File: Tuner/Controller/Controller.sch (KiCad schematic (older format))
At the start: 98 parts, among them J1 Conn_02x05_Odd_Even, J10 Conn_01x05, J11 Conn_Coaxial, J13 Conn_Coaxial, J15 Conn_01x02, J16 Conn_01x08, J18 Conn_01x01, J19 Conn_01x01, J2 Conn_02x05_Odd_Even, J20 Conn_01x01, J21 Conn_01x01, J3 Conn_02x05_Odd_Even, J4 Conn_02x05_Odd_Even, J5 Conn_02x05_Odd_Even, J6 Conn_01x02, J7 Conn_02x05_Odd_Even, J8 Conn_01x06, J9 Conn_Coaxial, Q10 2N7000, Q11 2N7000, Q12 2N7000, Q2 2N3904, Q9 2N7000, U4 LM350_TO220

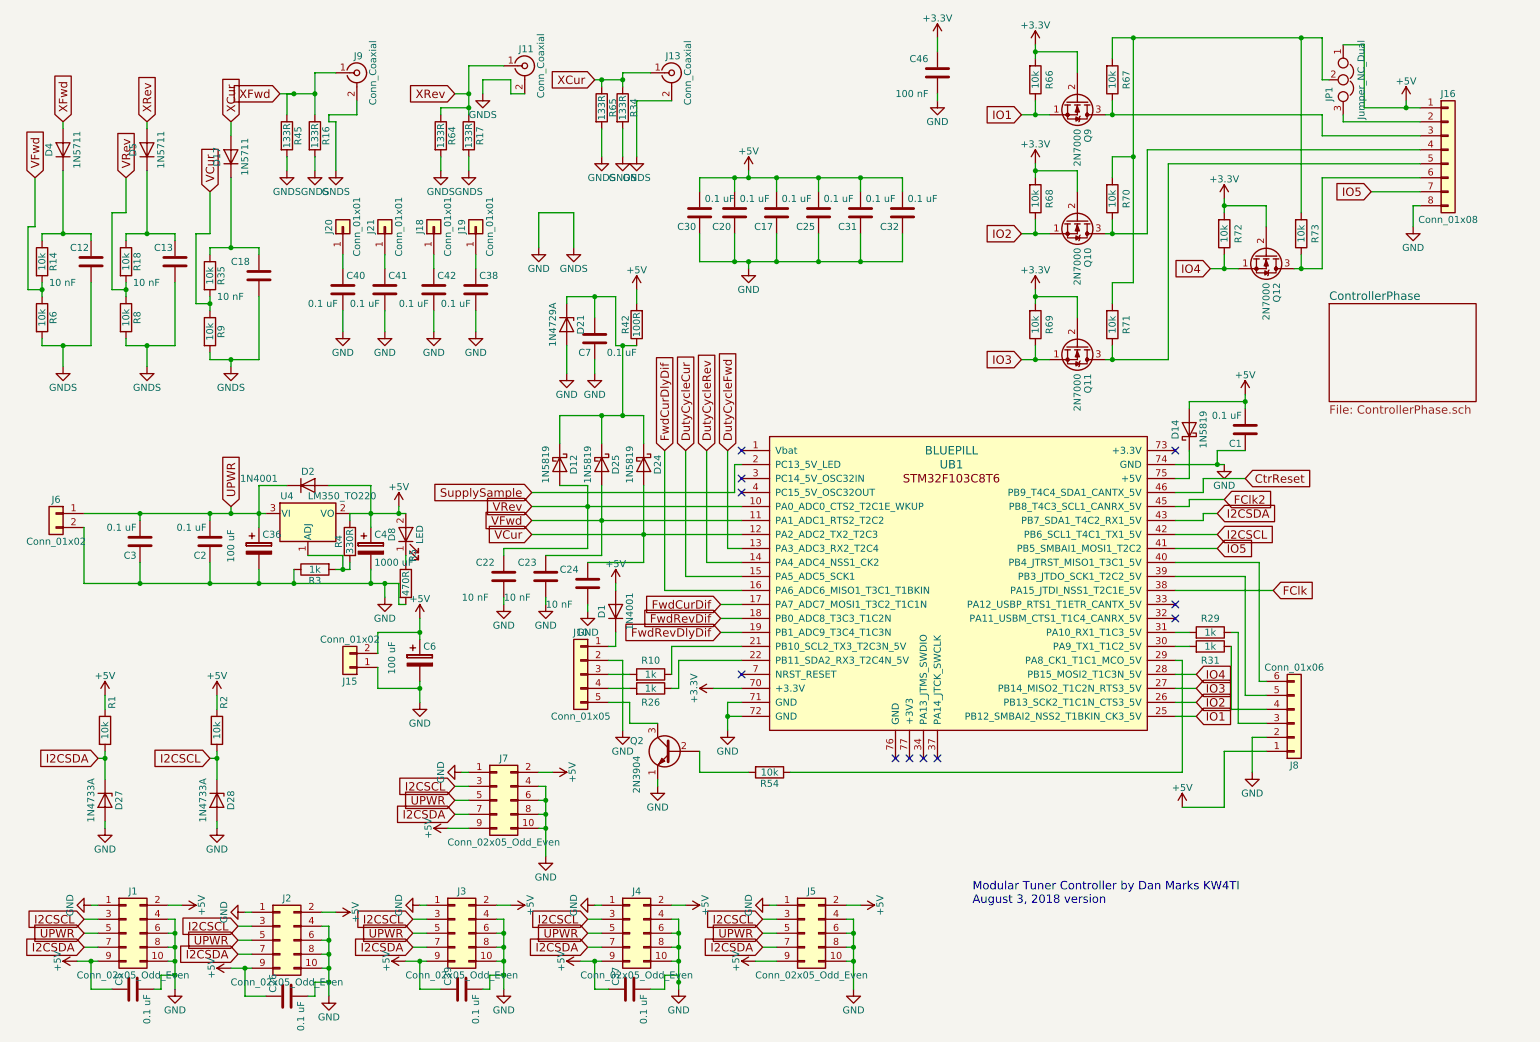
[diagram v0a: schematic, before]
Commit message: Changed I2C cable pinoutgit add Tunergit add Tuner Also added ICOM rig support
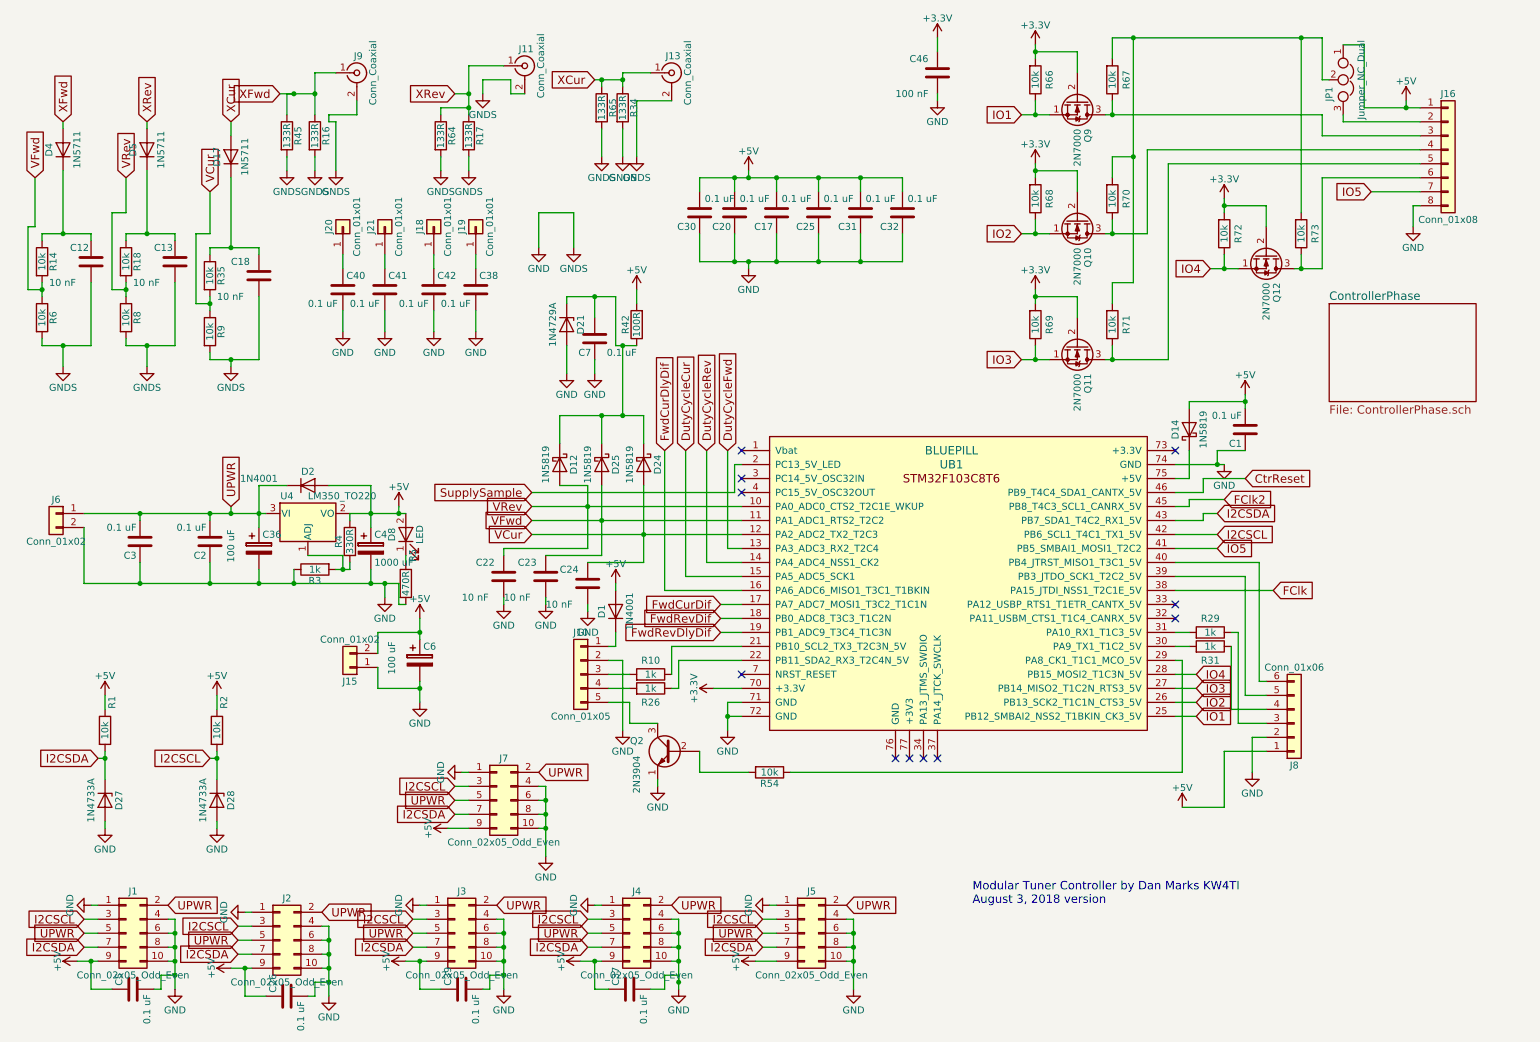
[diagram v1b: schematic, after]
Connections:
- net +5V: no longer J1.2 (Pin_2), J2.2 (Pin_2), J3.2 (Pin_2), J4.2 (Pin_2), J5.2 (Pin_2), J7.2 (Pin_2)
- net UPWR: now also J1.2 (Pin_2), J2.2 (Pin_2), J3.2 (Pin_2), J4.2 (Pin_2), J5.2 (Pin_2), J7.2 (Pin_2)

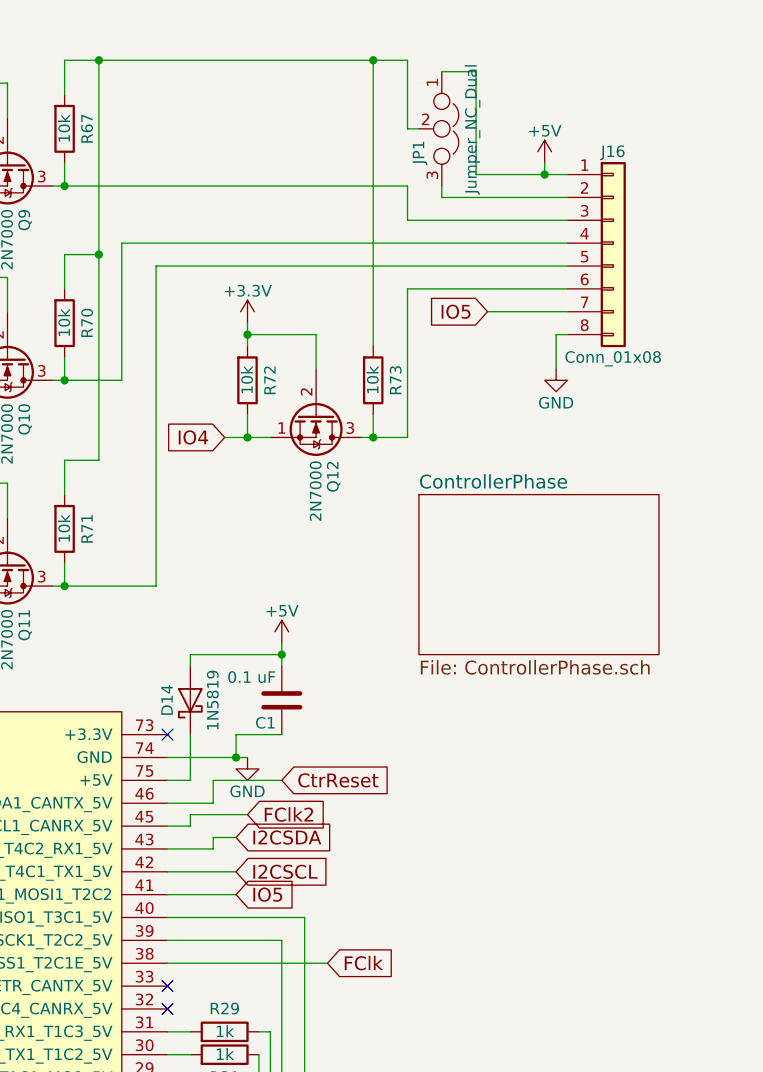
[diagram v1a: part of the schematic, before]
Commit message: Moved digital signal interface connector over
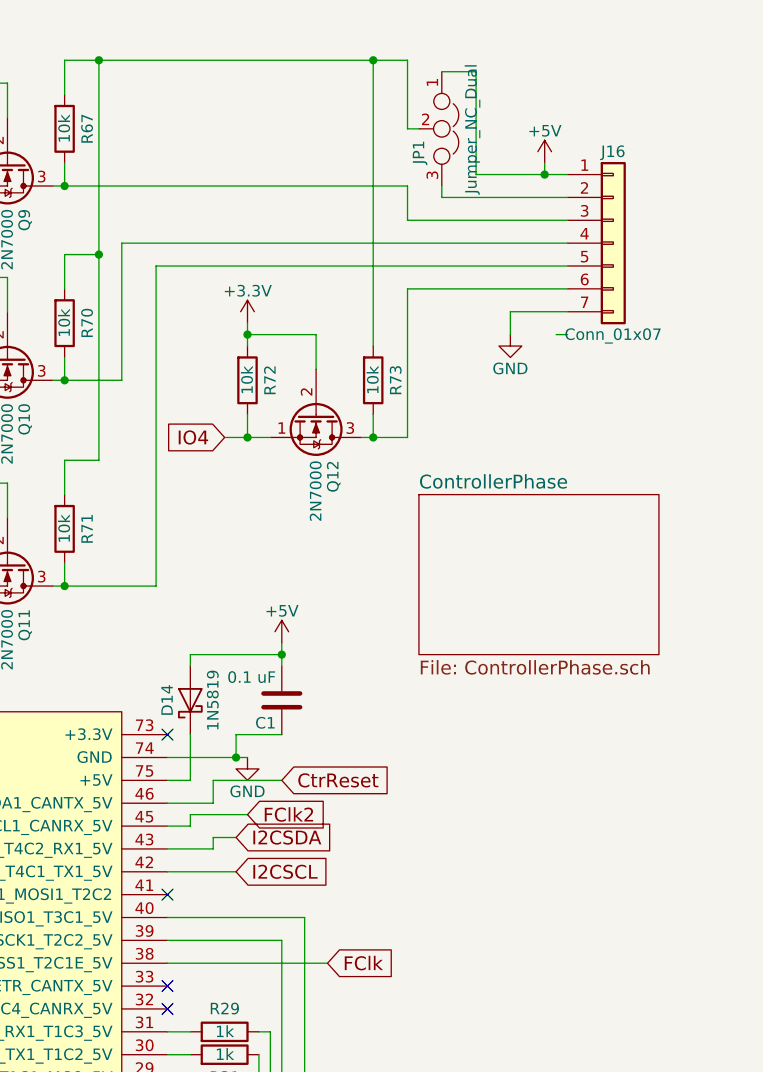
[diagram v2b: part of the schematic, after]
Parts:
- removed J16: Conn_01x08, Pin_Headers:Pin_Header_Straight_1x08_Pitch2.54mm, symbol Conn_01x08
- added J16: Conn_01x07, Pin_Headers:Pin_Header_Straight_1x07_Pitch2.54mm, symbol Conn_01x07
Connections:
- net +5V: now also J16.1 (Pin_1)
- net GND: now also J16.7 (Pin_7)
- net at JP1.3: now also J16.2 (Pin_2)
- net at Q9.3 (D), R67.1: now also J16.3 (Pin_3)
- net at Q10.3 (D), R70.1: now also J16.4 (Pin_4)
- net at Q11.3 (D), R71.1: now also J16.5 (Pin_5)
- net at Q12.3 (D), R73.1: now also J16.6 (Pin_6)
- net IO5: no longer names the net of UB1.41 (PB5_SMBAI1_MOSI1_T2C2)
- no-connect marks 11 -> 12
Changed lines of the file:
@@
 	1    0    0    -1
 $EndComp
-Text GLabel 9100 4250 2    60   Input ~ 0
-I2CSCL
 Text GLabel 1100 5850 0    60   Input ~ 0
 I2CSDA
@@
 	-1   0    0    1
 $EndComp
-Text GLabel 9100 4350 2    60   Input ~ 0
-IO5
-$Comp
-L Conn_01x08 J16
-U 1 1 5C87999F
-P 10750 1500
-F 0 "J16" H 10750 1900 50  0000 C CNN
-F 1 "Conn_01x08" H 10750 1000 50  0000 C CNN
-F 2 "Pin_Headers:Pin_Header_Straight_1x08_Pitch2.54mm" H 10750 1500 50  0001 C CNN
-F 3 "" H 10750 1500 50  0001 C CNN
-	1    10750 1500
-	1    0    0    -1
-$EndComp
 $Comp
 L 2N7000 Q9
@@
 L GND #PWR063
 U 1 1 5C87EAFE
-P 10500 2050
-F 0 "#PWR063" H 10500 1800 50  0001 C CNN
-F 1 "GND" H 10500 1900 50  0000 C CNN
-F 2 "" H 10500 2050 50  0001 C CNN
-F 3 "" H 10500 2050 50  0001 C CNN
-	1    10500 2050
+P 10300 1900
+F 0 "#PWR063" H 10300 1650 50  0001 C CNN
+F 1 "GND" H 10300 1750 50  0000 C CNN
+F 2 "" H 10300 1900 50  0001 C CNN
+F 3 "" H 10300 1900 50  0001 C CNN
+	1    10300 1900
 	1    0    0    -1
 $EndComp
@@
 Connection ~ 1400 4600
 Wire Wire Line
-	9100 4350 8800 4350
-Wire Wire Line
 	7700 1250 7900 1250
 Wire Wire Line
@@
 Wire Wire Line
 	8300 1250 9850 1250
-Wire Wire Line
-	10500 2050 10500 1900
 Wire Wire Line
 	10500 1900 10550 1900
@@
 Wire Wire Line
 	9850 1700 10550 1700
-Text GLabel 10200 1800 0    60   Input ~ 0
-IO5
-Wire Wire Line
-	10200 1800 10550 1800
 $Comp
 L GND #PWR067
@@
 Text GLabel 4250 5950 2    60   Input ~ 0
 UPWR
+$Comp
+L Conn_01x07 J16
+U 1 1 5DA6A74E
+P 10750 1500
+F 0 "J16" H 10750 1900 50  0000 C CNN
+F 1 "Conn_01x07" H 10750 1100 50  0000 C CNN
+F 2 "Pin_Headers:Pin_Header_Straight_1x07_Pitch2.54mm" H 10750 1500 50  0001 C CNN
+F 3 "" H 10750 1500 50  0001 C CNN
+	1    10750 1500
+	1    0    0    -1
+$EndComp
+Wire Wire Line
+	10300 1900 10300 1800
+Wire Wire Line
+	10300 1800 10550 1800
+Text GLabel 9100 4250 2    60   Input ~ 0
+I2CSCL
+NoConn ~ 8800 4350
 $EndSCHEMATC

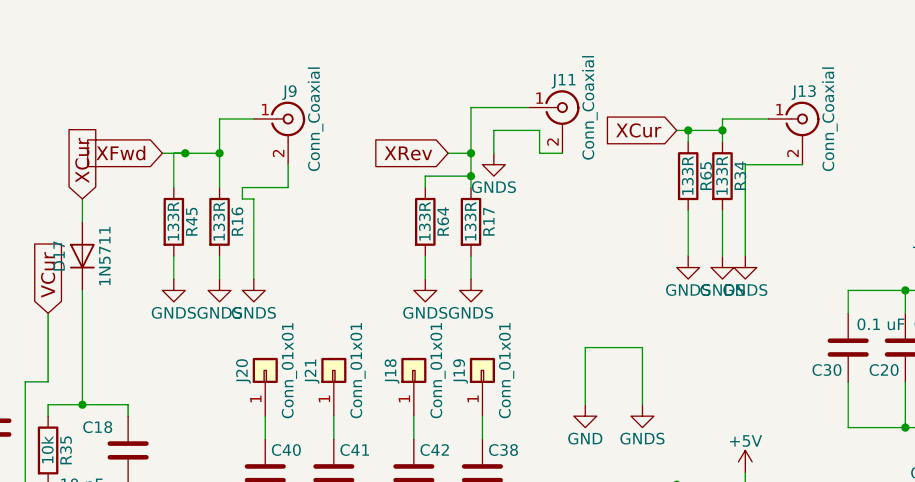
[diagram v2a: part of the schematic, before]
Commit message: Changed resistor values for termination
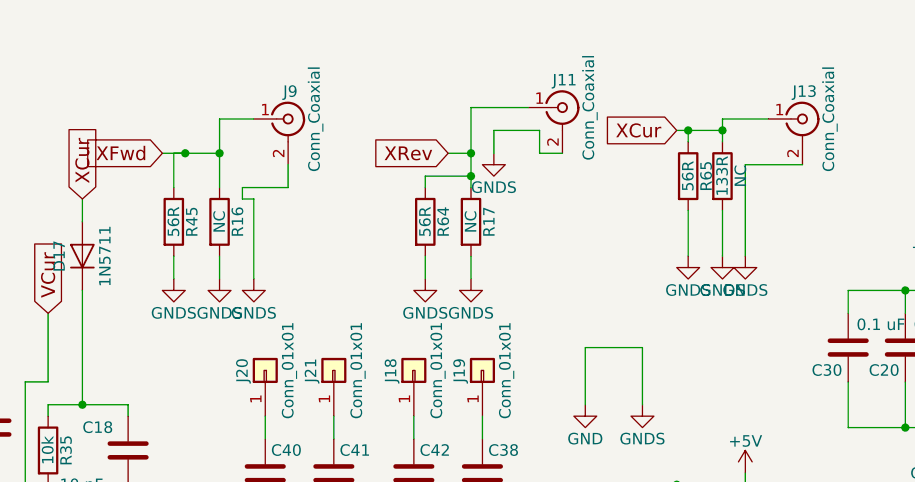
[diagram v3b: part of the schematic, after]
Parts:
- R16, R17: value 133R -> NC
- R45, R64, R65: value 133R -> 56R
- renumbered R34 to NC
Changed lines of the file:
@@
 P 2650 1400
 F 0 "R16" V 2730 1400 50  0000 C CNN
-F 1 "133R" V 2650 1400 50  0000 C CNN
+F 1 "NC" V 2650 1400 50  0000 C CNN
 F 2 "Resistors_THT:R_Axial_DIN0309_L9.0mm_D3.2mm_P12.70mm_Horizontal" V 2580 1400 50  0001 C CNN
 F 3 "" H 2650 1400 50  0001 C CNN
@@
 P 3750 1400
 F 0 "R17" V 3830 1400 50  0000 C CNN
-F 1 "133R" V 3750 1400 50  0000 C CNN
+F 1 "NC" V 3750 1400 50  0000 C CNN
 F 2 "Resistors_THT:R_Axial_DIN0309_L9.0mm_D3.2mm_P12.70mm_Horizontal" V 3680 1400 50  0001 C CNN
 F 3 "" H 3750 1400 50  0001 C CNN
@@
 $EndComp
 $Comp
-L R R34
+L R NC
 U 1 1 5B3E7157
 P 4850 1200
-F 0 "R34" V 4930 1200 50  0000 C CNN
+F 0 "NC" V 4930 1200 50  0000 C CNN
 F 1 "133R" V 4850 1200 50  0000 C CNN
 F 2 "Resistors_THT:R_Axial_DIN0309_L9.0mm_D3.2mm_P12.70mm_Horizontal" V 4780 1200 50  0001 C CNN
@@
 P 2450 1400
 F 0 "R45" V 2530 1400 50  0000 C CNN
-F 1 "133R" V 2450 1400 50  0000 C CNN
+F 1 "56R" V 2450 1400 50  0000 C CNN
 F 2 "Resistors_THT:R_Axial_DIN0309_L9.0mm_D3.2mm_P12.70mm_Horizontal" V 2380 1400 50  0001 C CNN
 F 3 "" H 2450 1400 50  0001 C CNN
@@
 P 3550 1400
 F 0 "R64" V 3630 1400 50  0000 C CNN
-F 1 "133R" V 3550 1400 50  0000 C CNN
+F 1 "56R" V 3550 1400 50  0000 C CNN
 F 2 "Resistors_THT:R_Axial_DIN0309_L9.0mm_D3.2mm_P12.70mm_Horizontal" V 3480 1400 50  0001 C CNN
 F 3 "" H 3550 1400 50  0001 C CNN
@@
 P 4700 1200
 F 0 "R65" V 4780 1200 50  0000 C CNN
-F 1 "133R" V 4700 1200 50  0000 C CNN
+F 1 "56R" V 4700 1200 50  0000 C CNN
 F 2 "Resistors_THT:R_Axial_DIN0309_L9.0mm_D3.2mm_P12.70mm_Horizontal" V 4630 1200 50  0001 C CNN
 F 3 "" H 4700 1200 50  0001 C CNN
